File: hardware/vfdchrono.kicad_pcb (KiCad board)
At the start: 2 copper layers, 30 parts, among them U1 LM2733YMF, U2 LM4871MX_NOPB, U3 IVL2-5_7, U4 HV5812WG

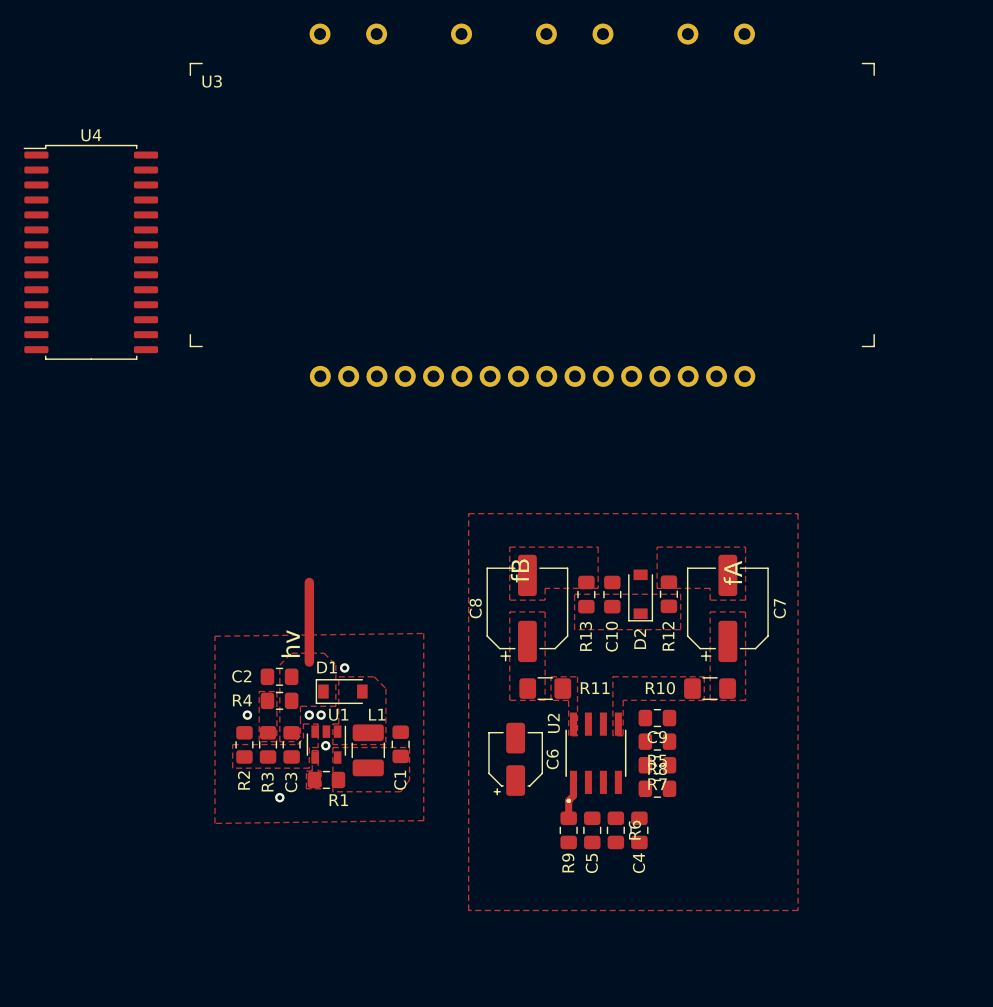
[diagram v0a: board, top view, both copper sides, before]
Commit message: further psu layout optimizations
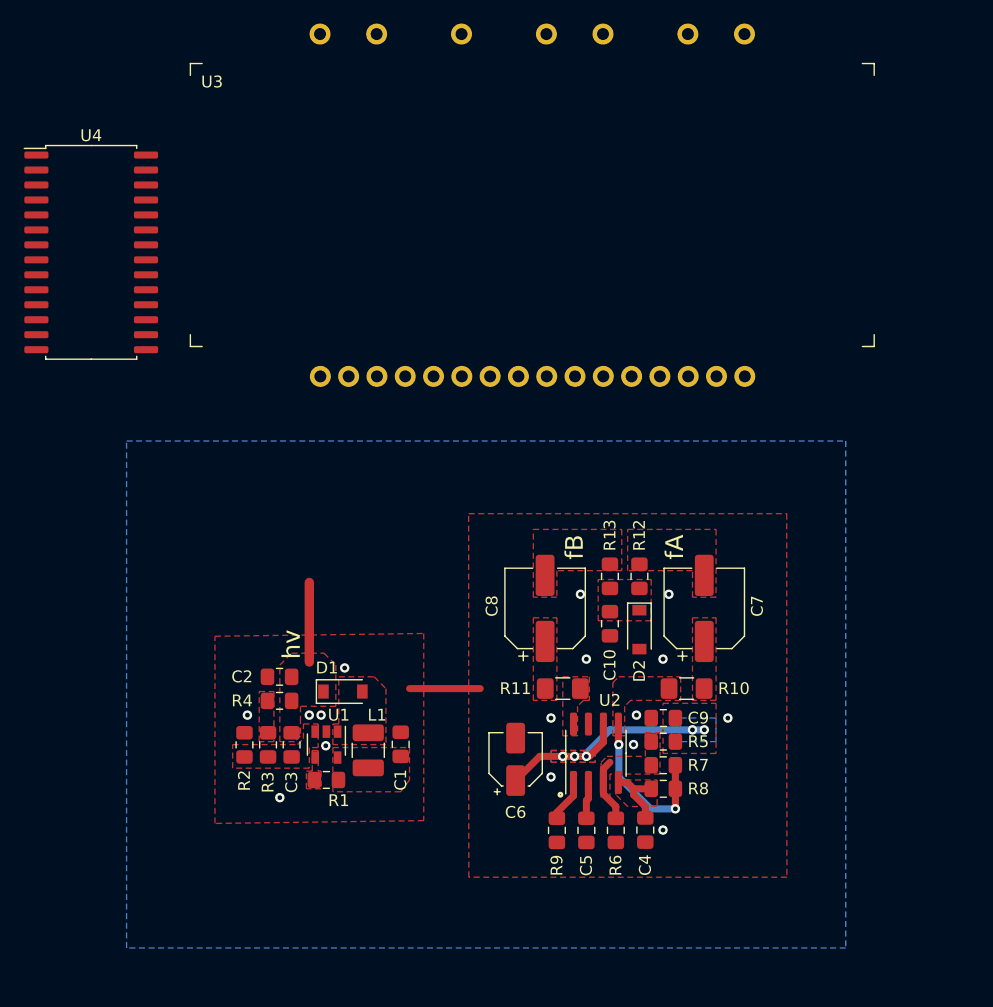
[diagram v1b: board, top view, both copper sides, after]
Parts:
- U2: footprint snapeda_lib:SOIC127P599X175-8N -> Package_SO:SOIC-8_3.9x4.9mm_P1.27mm
- moved D2 3.00 mm to (134.5, 60.0), turned to 270 degrees
- moved R12 2.93 mm to (134.5, 55.5)
- moved R13 2.53 mm to (132.0, 55.5)
- moved C10 2.48 mm to (132.0, 59.5), turned to 270 degrees
- moved C7 2.00 mm to (140.0, 58.2)
- moved R10 1.99 mm to (138.5, 65.0)
- moved C8 1.50 mm to (126.5, 58.2)
- moved R11 1.49 mm to (128.0, 65.0)
- moved R9 1.00 mm to (127.5, 77.0)
- moved C4 0.50 mm to (135.0, 77.0)
- moved C5 0.50 mm to (130.0, 77.0)
- moved C9 0.50 mm to (136.5, 67.5)
- moved R5 0.50 mm to (136.5, 69.5)
- moved R7 0.50 mm to (136.5, 71.5)
- moved R8 0.50 mm to (136.5, 73.5)
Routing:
- net /Universal VFD PSU by Rolo Kamp/5V: track 0.00 -> 21.4 mm, vias 0 -> 5
- net Net-(R10-Pad2): track 0.00 -> 14.1 mm, vias 0 -> 2
- net GND: track 0.00 -> 6.00 mm, vias 6 -> 16
- net Net-(C4-Pad1): track 0.00 -> 5.90 mm
- net Net-(R5-Pad2): track 0.00 -> 5.42 mm
- net Net-(C5-Pad1): track 0.00 -> 3.11 mm
- added copper zone on B.Cu, net /Universal VFD PSU by Rolo Kamp/5V
- added copper zone on B.Cu, net GND
- added copper zone on F.Cu, net Net-(C4-Pad1)
- added copper zone on F.Cu, net Net-(R5-Pad2)

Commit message: commit the board version that went to aisler, more silkscreen info
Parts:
- removed the U1 at (108.0, 69.8)
- added H1: MountingHole_Pad, MountingHole:MountingHole_2.7mm_M2.5_Pad, F.Cu at (90.0, 52.5)
- added H2: MountingHole_Pad, MountingHole:MountingHole_2.7mm_M2.5_Pad, F.Cu at (90.0, 82.5)
- added H3: MountingHole_Pad, MountingHole:MountingHole_2.7mm_M2.5_Pad, F.Cu at (155.0, 52.5)
- added H4: MountingHole_Pad, MountingHole:MountingHole_2.7mm_M2.5_Pad, F.Cu at (155.0, 82.5)
- added J1: Connection Header, Connector_PinHeader_2.54mm:PinHeader_1x08_P2.54mm_Vertical, F.Cu at (90.0, 58.5)
- added R14: 4.7kΩ, Resistor_SMD:R_0805_2012Metric_Pad1.15x1.40mm_HandSolder, F.Cu at (105.2, 73.0)
- added U3: LM2733YMF, Package_TO_SOT_SMD:SOT-23-5, F.Cu at (100.2, 66.7)
- U1: renamed from U3; moved to B.Cu
- moved U1 87.6 mm to (162.0, 50.0), turned to 180 degrees
- moved U4 49.9 mm to (118.5, 67.5), turned to 270 degrees
- moved R9 28.4 mm to (155.5, 72.5), turned to 0 degrees
- moved C5 26.5 mm to (155.5, 70.0), turned to 0 degrees
- moved C6 26.0 mm to (149.5, 76.0), turned to 180 degrees
- moved R6 24.9 mm to (155.5, 67.5), turned to 0 degrees
- moved C4 23.8 mm to (155.5, 65.0), turned to 0 degrees
- moved R8 18.4 mm to (152.0, 63.5), turned to 90 degrees
- moved C8 18.4 mm to (136.7, 73.5), turned to 180 degrees
- moved U2 18.2 mm to (149.0, 69.2), turned to 180 degrees
- moved R11 17.0 mm to (143.5, 72.0), turned to 90 degrees
- moved R7 15.7 mm to (150.0, 63.5), turned to 270 degrees
- moved C1 14.4 mm to (100.3, 73.0), turned to 0 degrees
- moved R5 13.0 mm to (148.0, 63.5), turned to 270 degrees
- moved R13 12.7 mm to (134.0, 68.0), turned to 180 degrees
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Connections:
- net /Universal VFD PSU by Rolo Kamp/FIL_SHDN renamed FIL_SHDN
- C1 pad 1: /Universal VFD PSU by Rolo Kamp/5V -> +5V
- C6 pad 1: /Universal VFD PSU by Rolo Kamp/5V -> +5V
- C7 pad 2: FILAMENT+ -> FILAMENT-
- C8 pad 2: FILAMENT- -> FILAMENT+
- C9 pad 1: /Universal VFD PSU by Rolo Kamp/5V -> +5V
- L1 pad 1: /Universal VFD PSU by Rolo Kamp/5V -> +5V
- R1 pad 1: /Universal VFD PSU by Rolo Kamp/5V -> +5V
- R1 pad 2: /Universal VFD PSU by Rolo Kamp/~HV_SHDN~ -> ~HV_SHDN~
- R12 pad 2: FILAMENT+ -> FILAMENT-
- R13 pad 2: FILAMENT- -> FILAMENT+
- R5 pad 1: /Universal VFD PSU by Rolo Kamp/5V -> +5V
- U1 pad 10: (no net) -> /d
- U1 pad 11: (no net) -> /G4
- U1 pad 12: (no net) -> /b
- U1 pad 13: (no net) -> /f
- U1 pad 14: (no net) -> /a
- U1 pad 15: (no net) -> /G5
- U1 pad 2: (no net) -> /G1
- U1 pad 3: (no net) -> /dt
- U1 pad 4: (no net) -> /g
- U1 pad 5: (no net) -> /e
- U1 pad 6: (no net) -> /G2
- U1 pad 7: (no net) -> /c
- U1 pad 8: (no net) -> /G3
- U1 pad 9: (no net) -> /db
- U2 pad 6: /Universal VFD PSU by Rolo Kamp/5V -> +5V
- U4 pad 10: (no net) -> /dt
- U4 pad 11: (no net) -> /g
- U4 pad 12: (no net) -> /e
- U4 pad 13: (no net) -> HV_BLANK
- U4 pad 15: (no net) -> HV_CLOCK
- U4 pad 16: (no net) -> HV_STROBE
- U4 pad 17: (no net) -> /G5
- U4 pad 18: (no net) -> /a
- U4 pad 19: (no net) -> /f
- U4 pad 20: (no net) -> /b
- U4 pad 21: (no net) -> /G4
- U4 pad 22: (no net) -> /d
- U4 pad 23: (no net) -> /db
- U4 pad 24: (no net) -> /G3
- U4 pad 25: (no net) -> /c
- U4 pad 26: (no net) -> /G2
- U4 pad 27: (no net) -> HV_DATA
- U4 pad 28: (no net) -> +5V
- U4 pad 9: (no net) -> /G1
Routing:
- net +5V: track 0.00 -> 121.4 mm, vias 0 -> 8
- net FIL_SHDN: track 3.62 -> 84.8 mm, vias 0 -> 1
- net FILAMENT-: track 0.00 -> 62.0 mm, vias 0 -> 3
- net HV_DATA: track 0.00 -> 38.6 mm, vias 0 -> 2
- net ~HV_SHDN~: track 0.00 -> 36.9 mm, vias 0 -> 2
- net /G1: track 0.00 -> 34.0 mm, vias 0 -> 2
- net /dt: track 0.00 -> 33.0 mm, vias 0 -> 2
- net FILAMENT+: track 0.00 -> 32.2 mm, vias 0 -> 1
- net HV_BLANK: track 0.00 -> 32.0 mm
- net /g: track 0.00 -> 31.9 mm, vias 0 -> 2
- net /e: track 0.00 -> 31.3 mm, vias 0 -> 2
- net HV_STROBE: track 0.00 -> 30.0 mm, vias 0 -> 2
- net HV_CLOCK: track 0.00 -> 29.9 mm, vias 0 -> 2
- net /Universal VFD PSU by Rolo Kamp/5V: track 21.4 -> 0.00 mm, vias 5 -> 0
- net +24V: track 6.75 -> 26.0 mm
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- added copper zone on B.Cu, net +5V
- added copper zone on F.Cu, net +5V
- added copper zone on F.Cu, net ~HV_SHDN~
- removed copper zone on B.Cu, net /Universal VFD PSU by Rolo Kamp/5V
- removed copper zone on F.Cu, net /Universal VFD PSU by Rolo Kamp/5V
- removed copper zone on F.Cu, net /Universal VFD PSU by Rolo Kamp/~HV_SHDN~
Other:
- board outline added: 75 x 40 mm
- board text added: "1"
- board text added: "10"
- board text added: "11"
- board text added: "12"
- board text added: "13"
- board text added: "14"
- board text added: "2"
- board text added: "3"
- board text added: "4"
- board text added: "5"
- board text added: "5V"
- board text added: "6"
- board text added: "7"
- board text added: "8"
- board text added: "9"
- board text added: "G1"
- board text added: "G2"
- board text added: "G3"
- board text added: "G4"
- board text added: "G5"
- board text added: "GND"
- board text added: "HV5812"
- board text added: "M2.5"
- board text added: "VFD Driver Board v1.0 2020 ansemjo"
- board text added: "a"
- board text added: "b"
- board text added: "blank"
- board text added: "c"
- board text added: "clock"
- board text added: "d"
- board text added: "data"
- board text added: "db"
- board text added: "dt"
- board text added: "e"
- board text added: "f"
- board text added: "fil+"
- board text added: "fil-"
- board text added: "filShdn"
- board text added: "filament ac"
- board text added: "function:"
- board text added: "g"
- board text added: "high voltage"
- board text added: "hvout:"
- board text added: "strobe"
- board text added: "~hvShdn~"
- board text added: "Индикатор Вакуумный Люминесцентный ИВЛ2-7/5"
- board text removed: "fA"
- board text removed: "fB"
- board text removed: "hv"
